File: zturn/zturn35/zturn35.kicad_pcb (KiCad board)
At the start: 4 copper layers, 189.9 x 54 mm, 45 parts, among them Q1 SSM6N15AFU, Q10 SSM6N15AFU, Q11 SSM6N15AFU, Q12 SSM6N15AFU, Q13 SSM6N15AFU, Q14 SSM6N15AFU, Q15 SSM6N15AFU, Q2 SSM6N15AFU, Q3 SSM6N15AFU, Q4 SSM6N15AFU, Q5 SSM6N15AFU, Q6 SSM6N15AFU, Q7 SSM6N15AFU, Q8 SSM6N15AFU, Q9 SSM6N15AFU, U10 74AXP4T245, U11 74AXP4T245, U12 74AXP4T245, U9 74AXP4T245

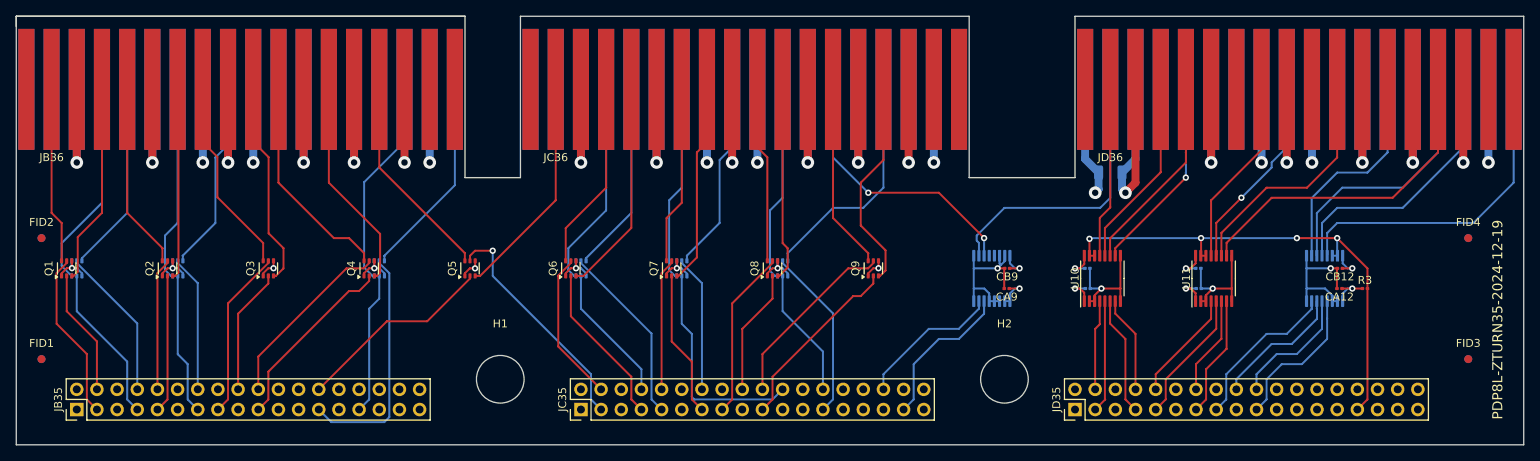
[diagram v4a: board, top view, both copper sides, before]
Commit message: update signals and zturn pcbs with pullups
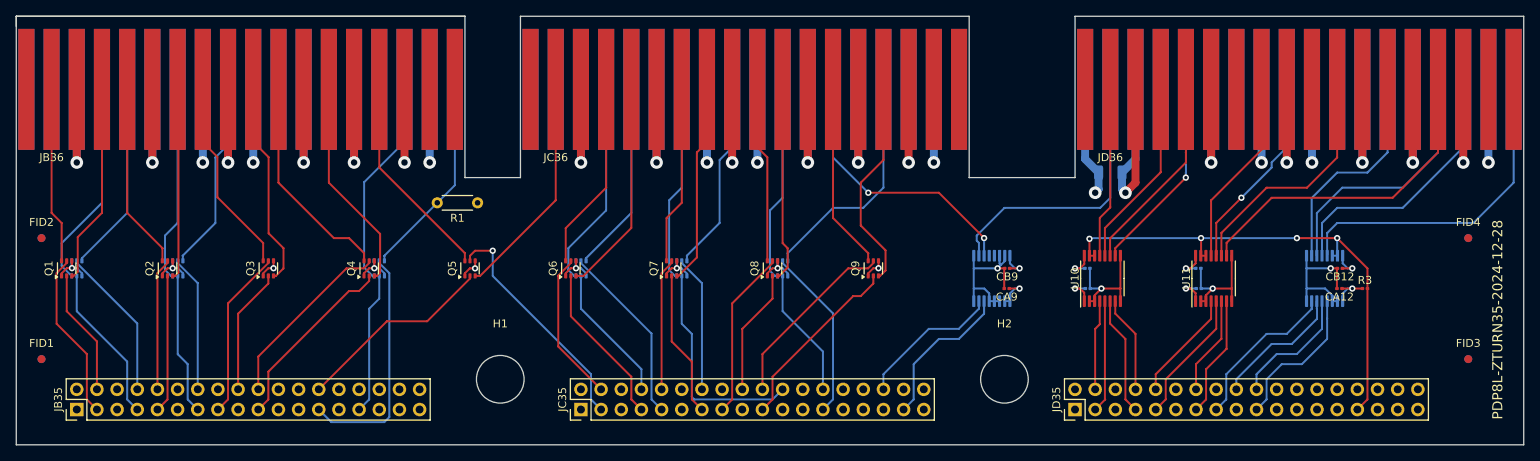
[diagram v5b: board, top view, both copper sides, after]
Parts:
- added R1: 1K, Resistor_THT:R_Axial_DIN0204_L3.6mm_D1.6mm_P5.08mm_Horizontal, F.Cu at (58.1, 23.5)
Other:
- board text added: "PDP8L-ZTURN35-2024-12-28"
- board text removed: "PDP8L-ZTURN35-2024-12-19"
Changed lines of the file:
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@@
+    )
+  )
+  (footprint "Resistor_THT:R_Axial_DIN0204_L3.6mm_D1.6mm_P5.08mm_Horizontal" (layer "F.Cu")
+    (at 58.1025 23.495 180)
+    (descr "Resistor, Axial_DIN0204 series, Axial, Horizontal, pin pitch=5.08mm, 0.167W, length*diameter=3.6*1.6mm^2, http://cdn-reichelt.de/documents/datenblatt/B400/1_4W%23YAG.pdf")
+    (tags "Resistor Axial_DIN0204 series Axial Horizontal pin pitch 5.08mm 0.167W length 3.6mm diameter 1.6mm")
+    (property "Sheetfile" "zturn35.kicad_sch")
+    (property "Sheetname" "")
+    (property "ki_description" "Resistor, US symbol")
+    (property "ki_keywords" "R res resistor")
+    (attr through_hole)
+    (fp_text reference "R1" (at 2.54 -1.92) (layer "F.SilkS")
+        (effects (font (size 1 1) (thickness 0.15)))
+    )
+    (fp_text value "1K" (at 2.54 1.92) (layer "F.Fab")
+        (effects (font (size 1 1) (thickness 0.15)))
+    )
+    (fp_text user "${REFERENCE}" (at 2.54 0) (layer "F.Fab")
+        (effects (font (size 0.72 0.72) (thickness 0.108)))
+    )
+    (fp_line (start 0.62 -0.92) (end 4.46 -0.92)
+      (stroke (width 0.12) (type solid)) (layer "F.SilkS"))
+    (fp_line (start 0.62 0.92) (end 4.46 0.92)
+      (stroke (width 0.12) (type solid)) (layer "F.SilkS"))
+    (fp_line (start -0.95 -1.05) (end -0.95 1.05)
+      (stroke (width 0.05) (type solid)) (layer "F.CrtYd"))
+    (fp_line (start -0.95 1.05) (end 6.03 1.05)
+      (stroke (width 0.05) (type solid)) (layer "F.CrtYd"))
+    (fp_line (start 6.03 -1.05) (end -0.95 -1.05)
+      (stroke (width 0.05) (type solid)) (layer "F.CrtYd"))
+    (fp_line (start 6.03 1.05) (end 6.03 -1.05)
+      (stroke (width 0.05) (type solid)) (layer "F.CrtYd"))
+    (fp_line (start 0 0) (end 0.74 0)
+      (stroke (width 0.1) (type solid)) (layer "F.Fab"))
+    (fp_line (start 0.74 -0.8) (end 0.74 0.8)
+      (stroke (width 0.1) (type solid)) (layer "F.Fab"))
+    (fp_line (start 0.74 0.8) (end 4.34 0.8)
+      (stroke (width 0.1) (type solid)) (layer "F.Fab"))
+    (fp_line (start 4.34 -0.8) (end 0.74 -0.8)
+      (stroke (width 0.1) (type solid)) (layer "F.Fab"))
+    (fp_line (start 4.34 0.8) (end 4.34 -0.8)
+      (stroke (width 0.1) (type solid)) (layer "F.Fab"))
+    (fp_line (start 5.08 0) (end 4.34 0)
+      (stroke (width 0.1) (type solid)) (layer "F.Fab"))
+    (pad "1" thru_hole circle (at 0 0 180) (size 1.4 1.4) (drill 0.7) (layers "*.Cu" "*.Mask")
+      (net 32 "+5V") (pintype "passive"))
+    (pad "2" thru_hole oval (at 5.08 0 180) (size 1.4 1.4) (drill 0.7) (layers "*.Cu" "*.Mask")
+      (net 113 "/j_EMA") (pintype "passive"))
+    (model "${KICAD6_3DMODEL_DIR}/Resistor_THT.3dshapes/R_Axial_DIN0204_L3.6mm_D1.6mm_P5.08mm_Horizontal.wrl"
+      (offset (xyz 0 0 0))
+      (scale (xyz 1 1 1))
+      (rotate (xyz 0 0 0))
     )
   )
@@
   (gr_line (start 189.865 53.975) (end 0 53.975)
     (stroke (width 0.1) (type default)) (layer "Edge.Cuts"))
-  (gr_text "PDP8L-ZTURN35-2024-12-19" (at 187.325 50.8 90) (layer "F.SilkS")
+  (gr_text "PDP8L-ZTURN35-2024-12-28" (at 187.325 50.8 90) (layer "F.SilkS")
     (effects (font (size 1.27 1.27) (thickness 0.15)) (justify left bottom))
   )

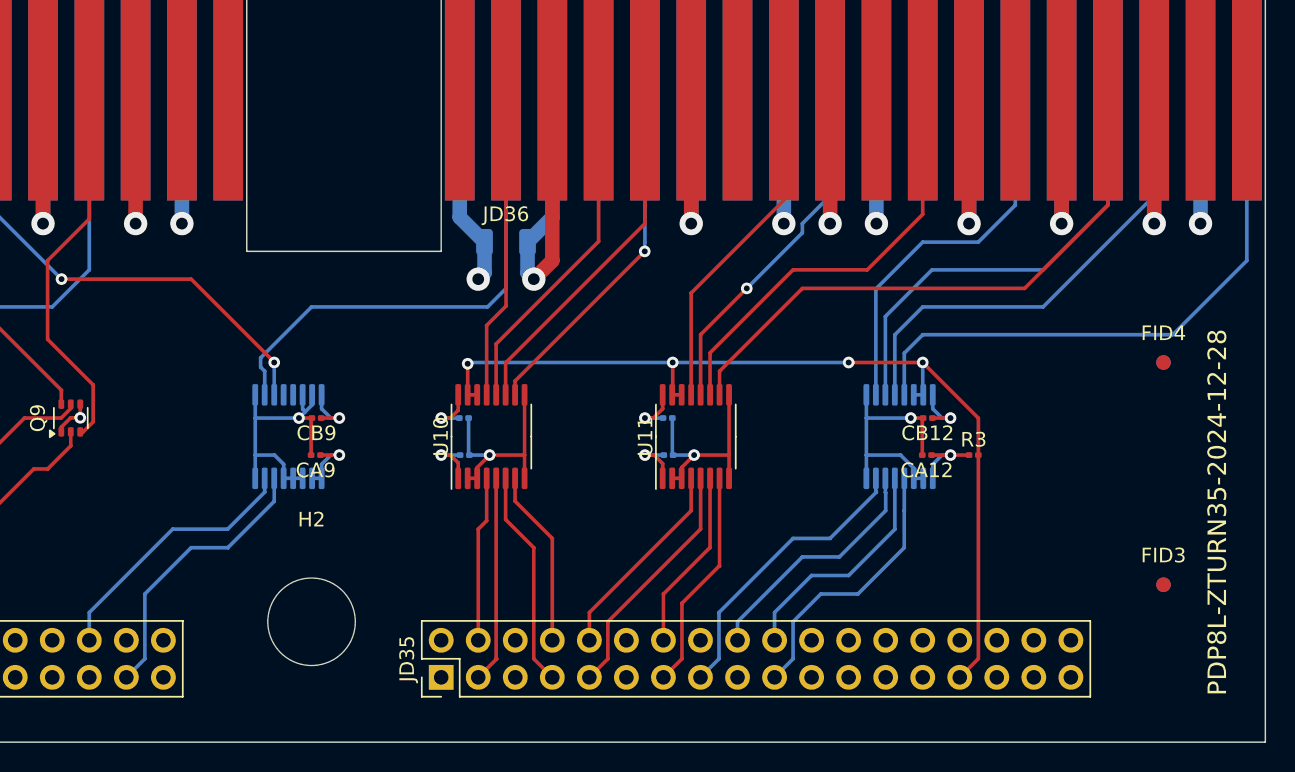
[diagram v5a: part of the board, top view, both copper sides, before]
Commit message: add I2C circuit to zturn boardset to operate front panel board
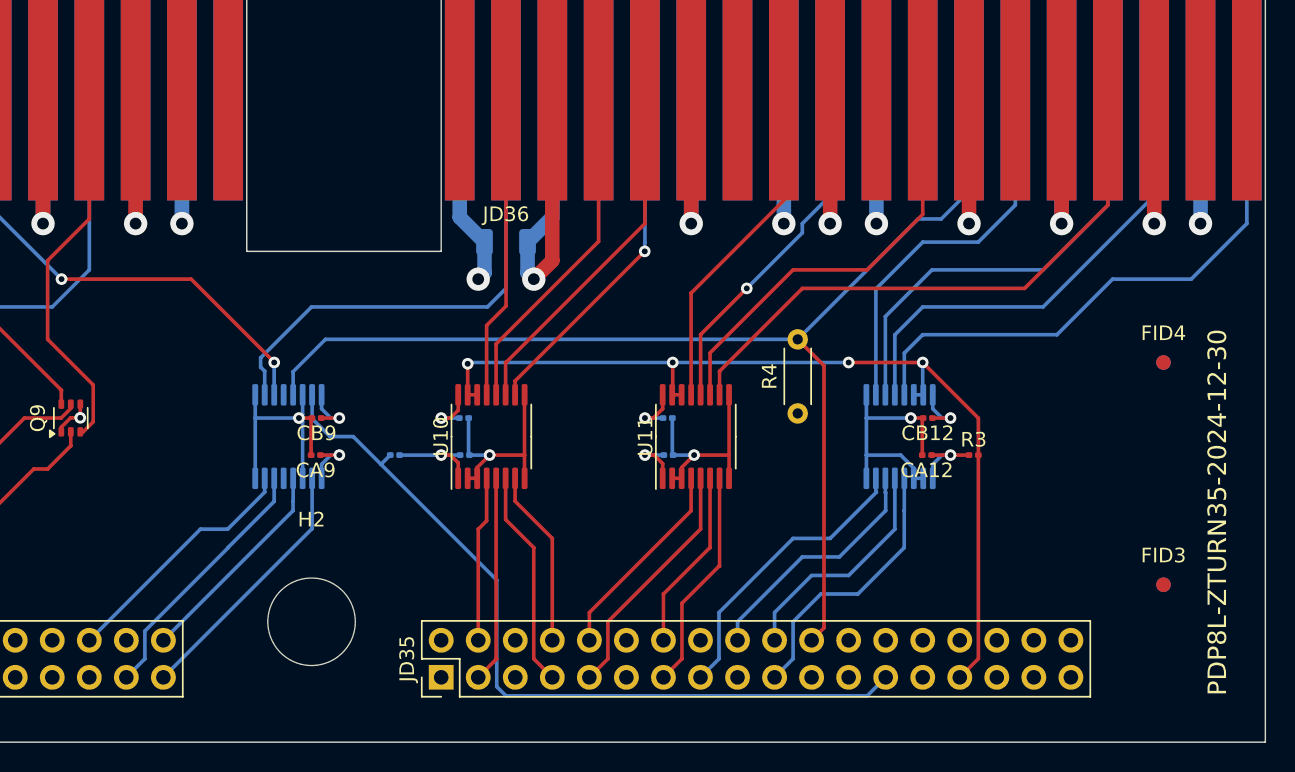
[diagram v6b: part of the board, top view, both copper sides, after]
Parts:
- added R2: 10K, Resistor_SMD:R_0201_0603Metric, B.Cu at (130.2, 34.3)
- added R4: 1K, Resistor_THT:R_Axial_DIN0204_L3.6mm_D1.6mm_P5.08mm_Horizontal, F.Cu at (157.8, 31.4)
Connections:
- JC35 pad 35: /i_EXTDMAADD_14 -> /FPI2CDDIR
- JC35 pad 36: /i_EXTDMAADD_13 -> /FPI2CDATA
- JD35 pad 22: unconnected-(JD35-Pin_22-Pad22) -> /EPI2CDAT
- JD35 pad 25: unconnected-(JD35-Pin_25-Pad25) -> /FPI2CDENA
- JD36 pad N2: GND -> /EPI2CDAT
- U9 pad 13: unconnected-(U9-1B1-Pad13) -> /EPI2CDAT
- U9 pad 15: GND -> /FPI2CDENA
- U9 pad 2: +3V3 -> /FPI2CDDIR
- U9 pad 4: GND -> /FPI2CDATA
- U9 pad 5: GND -> unconnected-(U9-1A2-Pad5)
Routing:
- net /EPI2CDAT: track 0.00 -> 74.8 mm
- net /FPI2CDENA: track 0.00 -> 54.5 mm
- net /FPI2CDDIR: track 0.00 -> 17.9 mm
- net /FPI2CDATA: track 0.00 -> 14.8 mm
- net GND: track 371.6 -> 364.2 mm
- net +3V3: track 16.9 -> 19.1 mm
- net /pBMB_11: track 40.7 -> 39.2 mm
- net /o_BWC_OVERFLOW: track 19.3 -> 17.8 mm
- net /oD35B2: track 18.3 -> 17.2 mm
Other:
- board text added: "PDP8L-ZTURN35-2024-12-30"
- board text removed: "PDP8L-ZTURN35-2024-12-28"

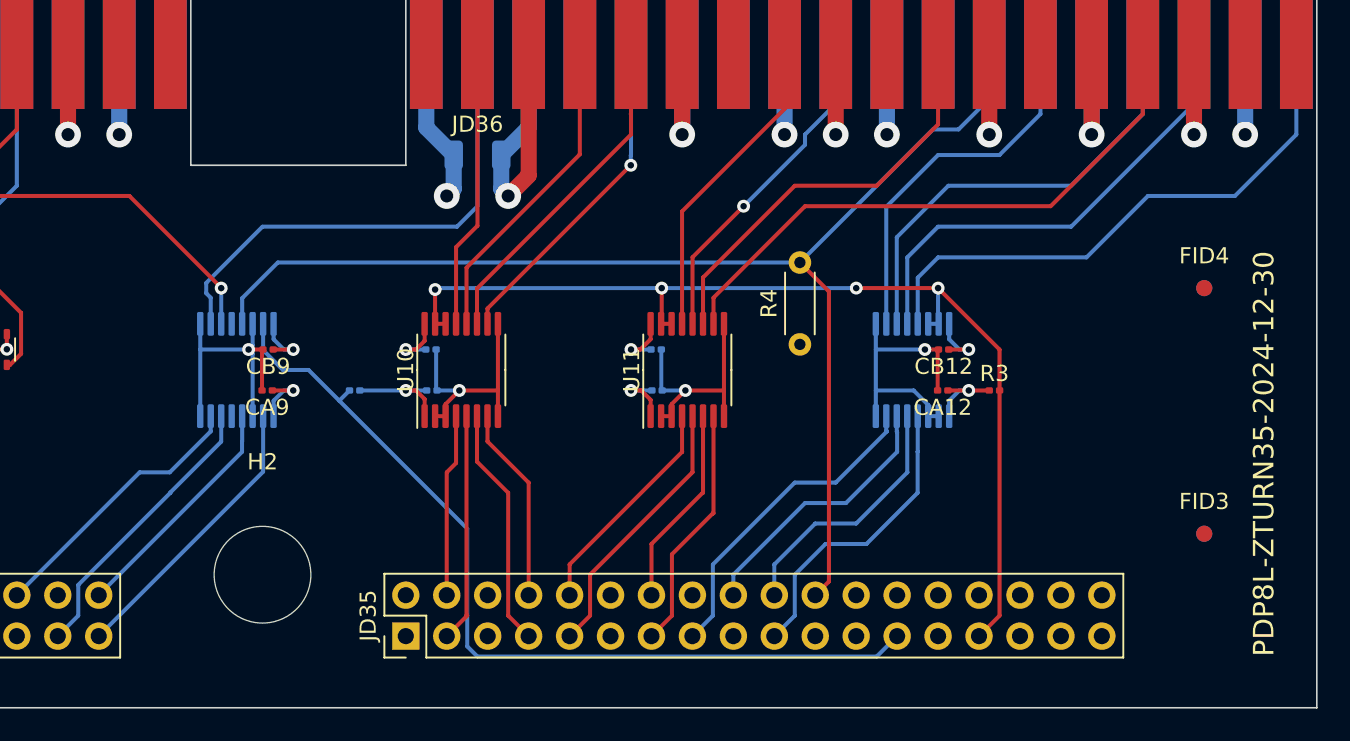
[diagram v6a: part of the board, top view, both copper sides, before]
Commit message: update zturn36,35 pcbs to put i2c at 3.3V and open-collector
...directly from FPGA pins with 2.2K pullups
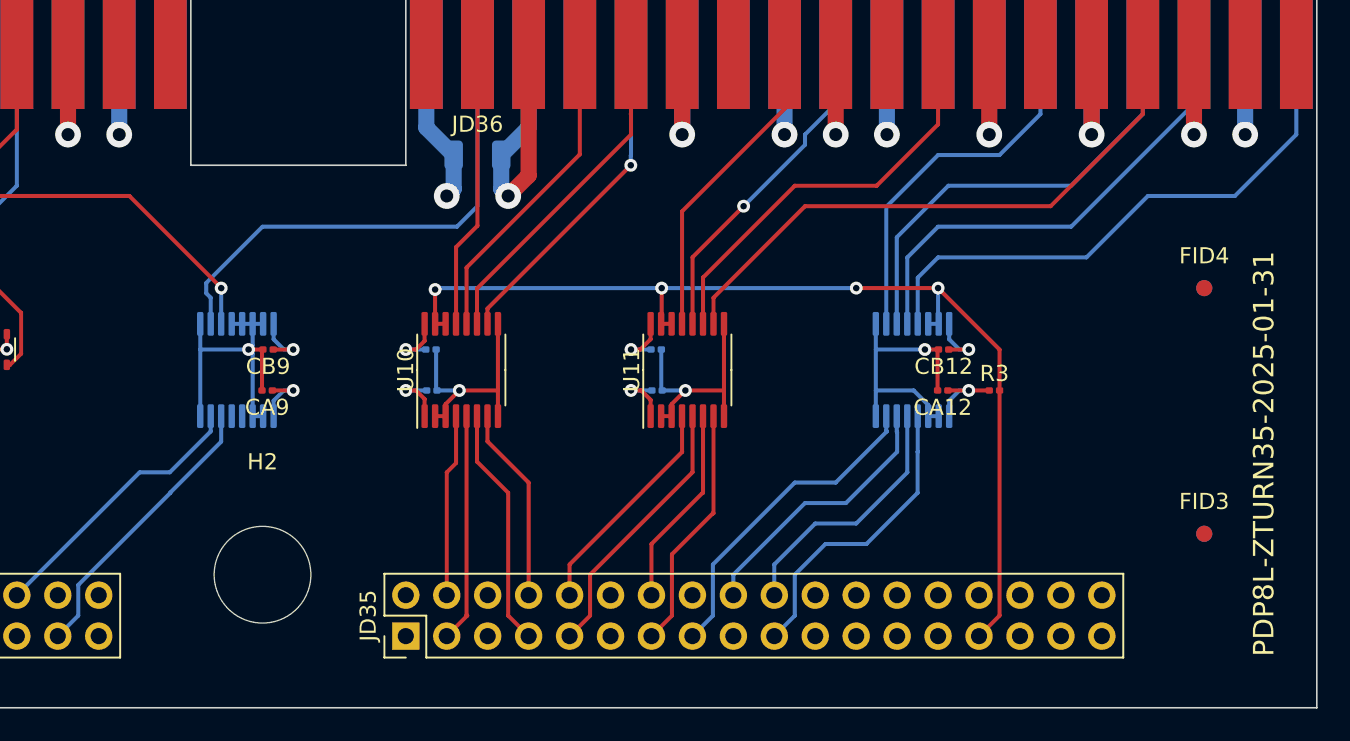
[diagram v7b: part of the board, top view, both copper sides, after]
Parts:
- removed R2: 10K, Resistor_SMD:R_0201_0603Metric
- removed R4: 1K, Resistor_THT:R_Axial_DIN0204_L3.6mm_D1.6mm_P5.08mm_Horizontal
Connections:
- JC35 pad 35: /FPI2CDDIR -> unconnected-(JC35-Pin_35-Pad35)
- JC35 pad 36: /FPI2CDATA -> unconnected-(JC35-Pin_36-Pad36)
- JD35 pad 22: /EPI2CDAT -> unconnected-(JD35-Pin_22-Pad22)
- JD35 pad 25: /FPI2CDENA -> unconnected-(JD35-Pin_25-Pad25)
- JD36 pad N2: /EPI2CDAT -> unconnected-(JD36-PadN2)
- U9 pad 12: unconnected-(U9-1B2-Pad12) -> GND
- U9 pad 13: /EPI2CDAT -> GND
- U9 pad 15: /FPI2CDENA -> GND
- U9 pad 2: /FPI2CDDIR -> GND
- U9 pad 4: /FPI2CDATA -> unconnected-(U9-1A1-Pad4)
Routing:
- net /EPI2CDAT: track 74.8 -> 0.00 mm
- net /FPI2CDENA: track 54.5 -> 0.00 mm
- net /FPI2CDDIR: track 17.9 -> 0.00 mm
- net /FPI2CDATA: track 14.8 -> 0.00 mm
- net +3V3: track 19.1 -> 16.2 mm
- net GND: track 364.2 -> 366.8 mm
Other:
- board text added: "PDP8L-ZTURN35-2025-01-31"
- board text removed: "PDP8L-ZTURN35-2024-12-30"

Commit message: put 2024-12-30 version of zturn35,36 boards back
the 2024-12-30 design had 5V I2C bus via 74AXP245s
the newer boards had 3.3V I2C bus directly on FPGA

the old boards work perfectly fine so go back to them
...rather than make new boards
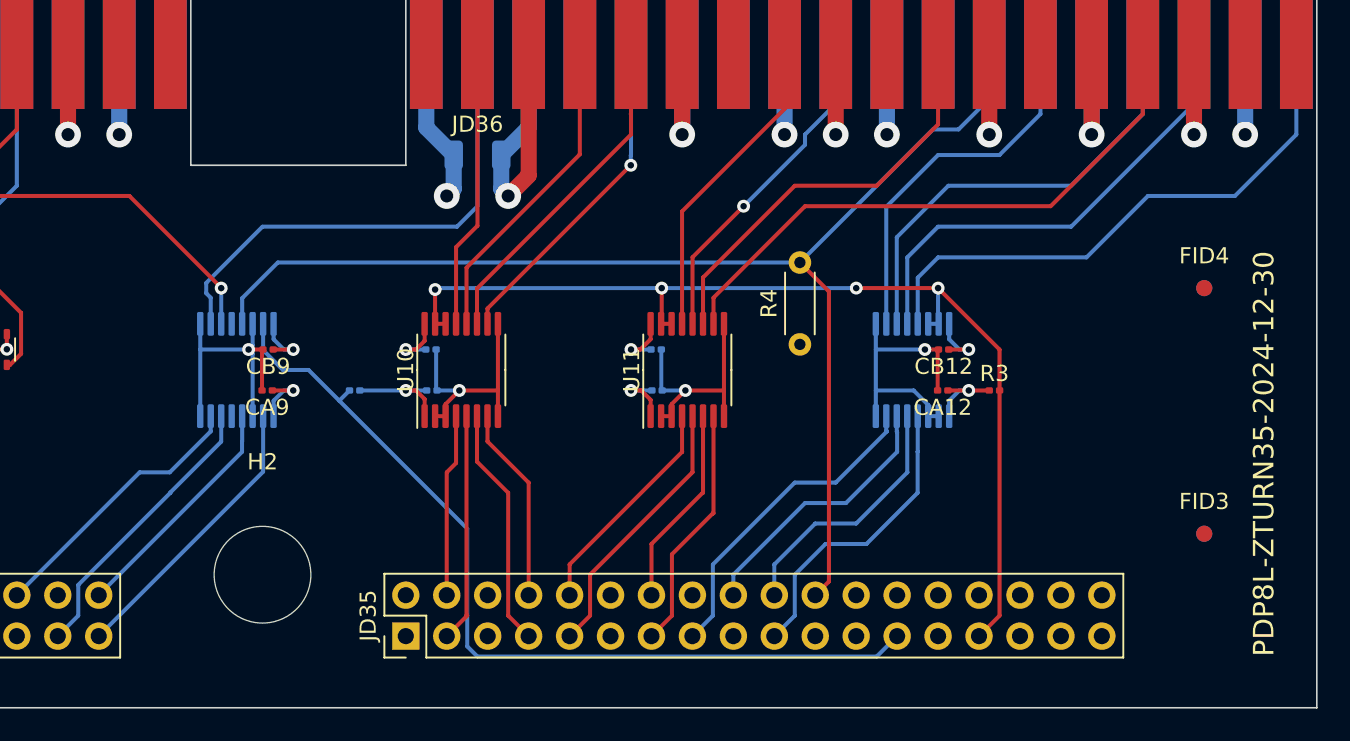
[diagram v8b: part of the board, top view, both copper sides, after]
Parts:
- added R2: 10K, Resistor_SMD:R_0201_0603Metric, B.Cu at (130.2, 34.3)
- added R4: 1K, Resistor_THT:R_Axial_DIN0204_L3.6mm_D1.6mm_P5.08mm_Horizontal, F.Cu at (157.8, 31.4)
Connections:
- JC35 pad 35: unconnected-(JC35-Pin_35-Pad35) -> /FPI2CDDIR
- JC35 pad 36: unconnected-(JC35-Pin_36-Pad36) -> /FPI2CDATA
- JD35 pad 22: unconnected-(JD35-Pin_22-Pad22) -> /EPI2CDAT
- JD35 pad 25: unconnected-(JD35-Pin_25-Pad25) -> /FPI2CDENA
- JD36 pad N2: unconnected-(JD36-PadN2) -> /EPI2CDAT
- U9 pad 12: GND -> unconnected-(U9-1B2-Pad12)
- U9 pad 13: GND -> /EPI2CDAT
- U9 pad 15: GND -> /FPI2CDENA
- U9 pad 2: GND -> /FPI2CDDIR
- U9 pad 4: unconnected-(U9-1A1-Pad4) -> /FPI2CDATA
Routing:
- net /EPI2CDAT: track 0.00 -> 74.8 mm
- net /FPI2CDENA: track 0.00 -> 54.5 mm
- net /FPI2CDDIR: track 0.00 -> 17.9 mm
- net /FPI2CDATA: track 0.00 -> 14.8 mm
- net +3V3: track 16.2 -> 19.1 mm
- net GND: track 366.8 -> 364.2 mm
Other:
- board text added: "PDP8L-ZTURN35-2024-12-30"
- board text removed: "PDP8L-ZTURN35-2025-01-31"
